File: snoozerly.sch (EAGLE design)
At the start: 49 parts, among them Q1 MOSFET_PCHANNEL, Q2 MOSFET-NCHANNELFDD8780, Q3 MOSFET-NCHANNELBSS123LT1G, Q4 MOSFET-NCHANNELBSS123LT1G, U1 ATMEGA328P, Y1 32KHz, Y2 8MHz

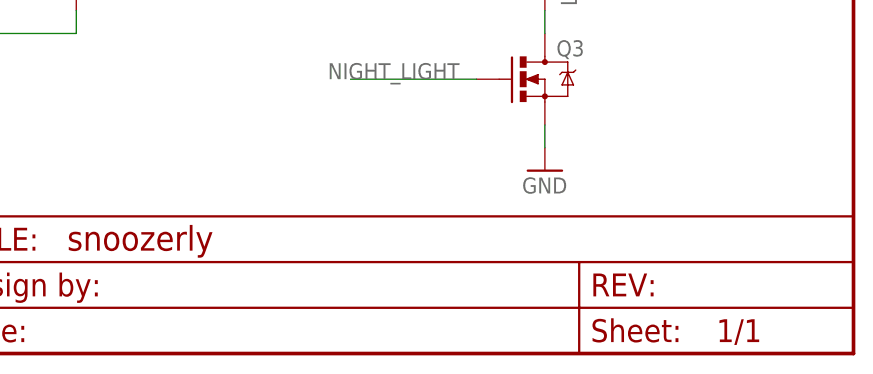
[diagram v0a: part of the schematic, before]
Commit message: renamed board and schematic files
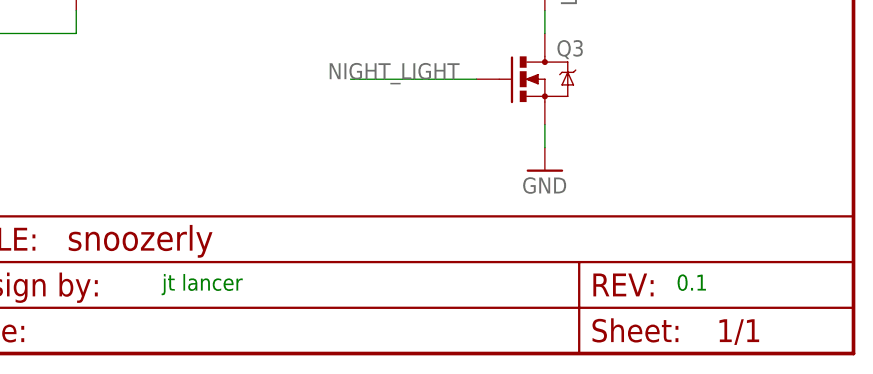
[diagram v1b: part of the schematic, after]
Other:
- note added: "0.1"
- note added: "jt lancer"
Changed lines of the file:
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@@
 <sheet>
 <plain>
+<text x="187.325" y="116.205" size="1.778" layer="91">jt lancer</text>
+<text x="244.475" y="116.205" size="1.778" layer="91">0.1</text>
 </plain>
 <instances>

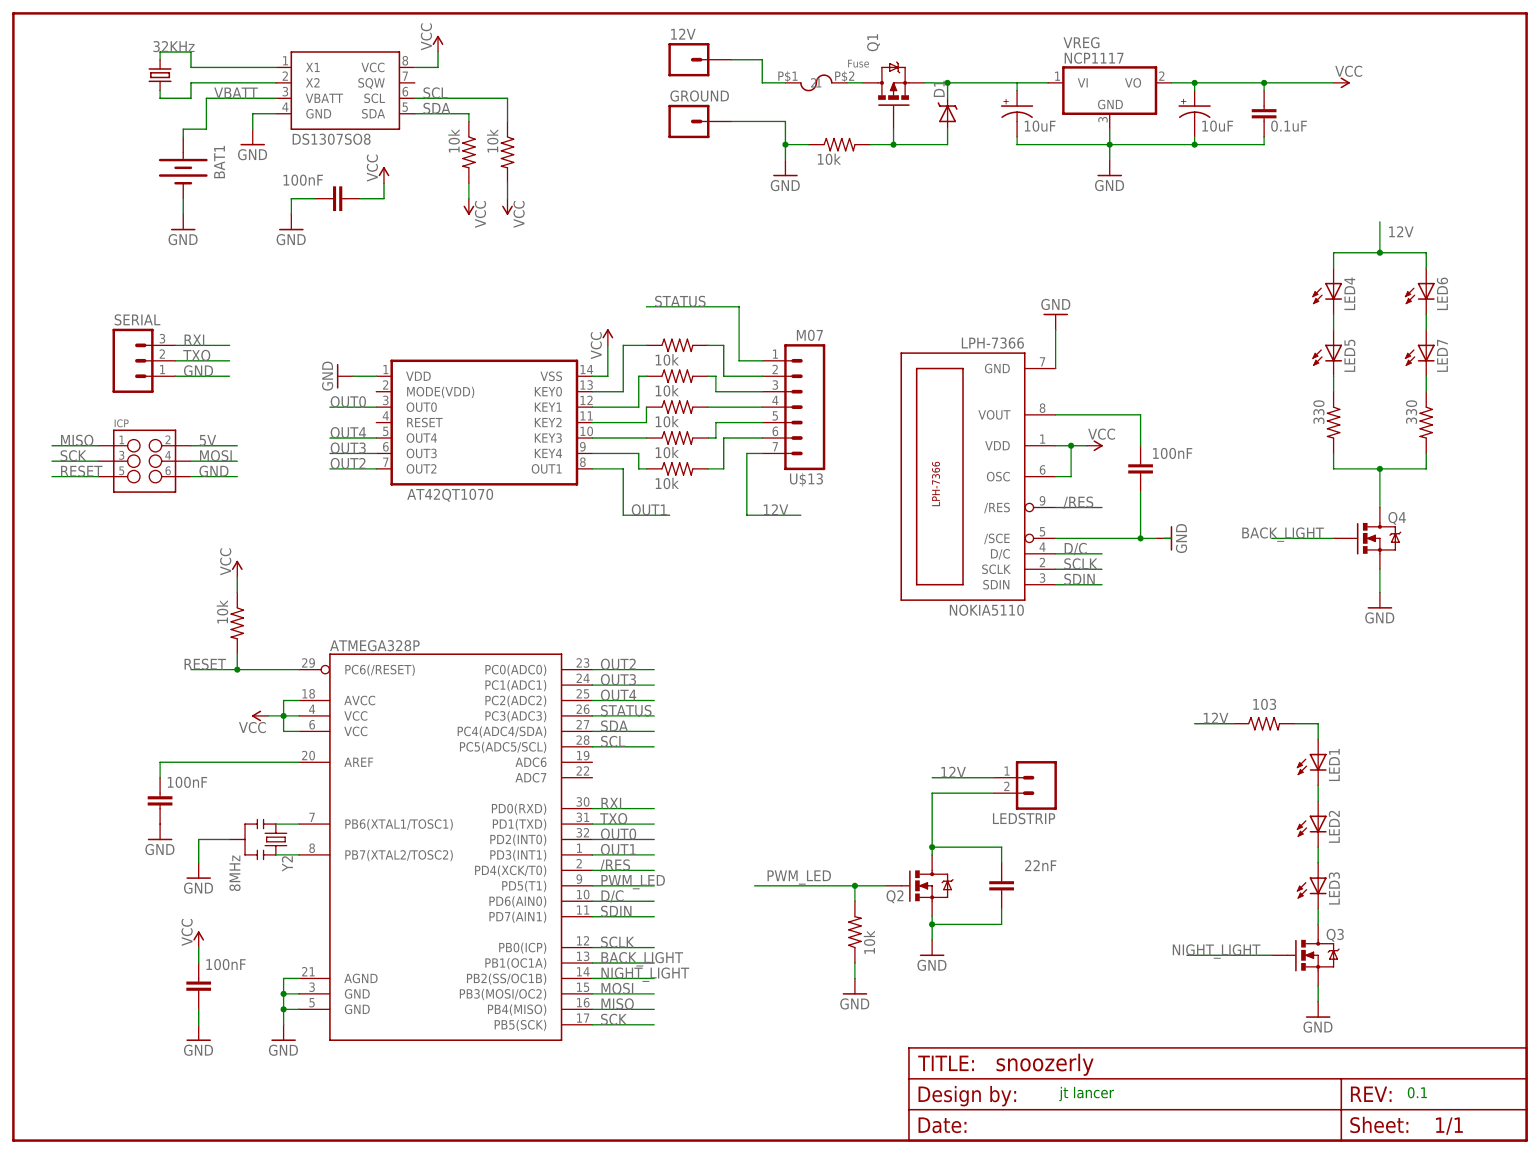
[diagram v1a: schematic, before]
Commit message: added output 0603 pullup resistors to touch sensor.
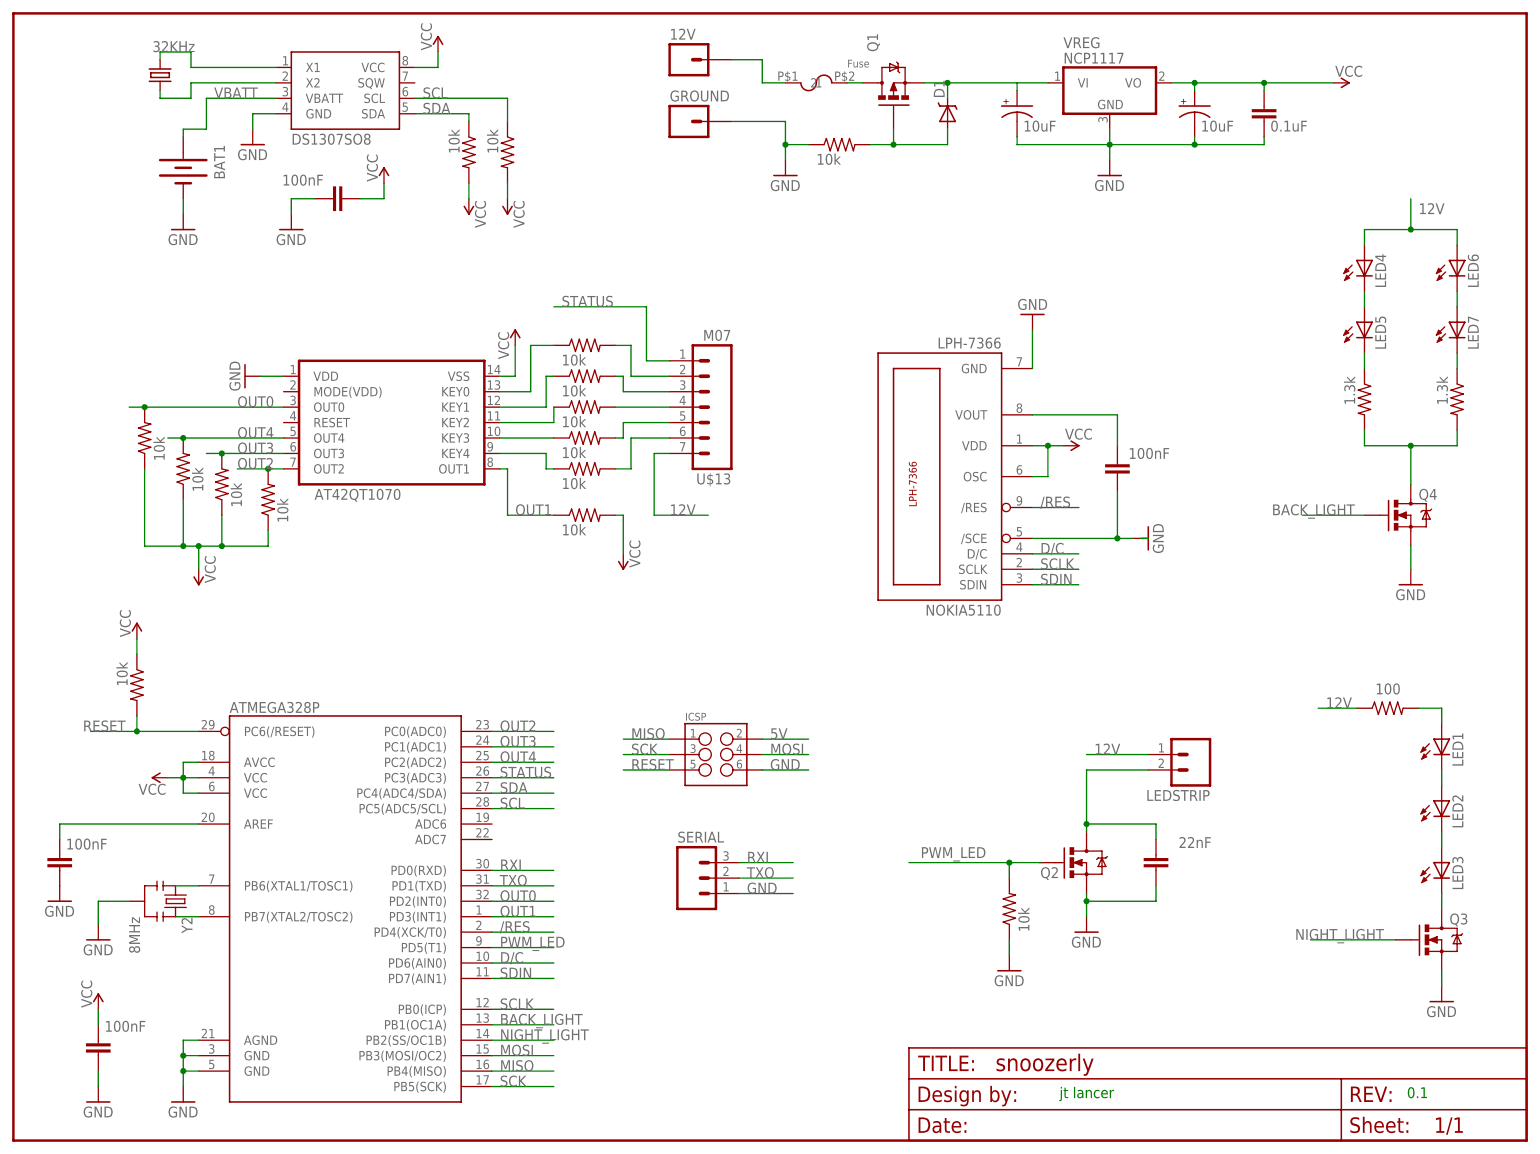
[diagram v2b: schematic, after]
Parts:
- removed ICP: (no value), SparkFun-Connectors:M03X2POGO_PINS
- added ICSP: (no value), SparkFun-Connectors:M03X2POGO_PINS
- added U$21, U$22, U$23, U$24, U$6: 10k, adafruit:R-US_R0603
- U$10, U$11, U$7, U$8, U$9: device jt_parts:RESISTOR -> adafruit:R-US_R0603
- U$16: value 103 -> 100
- U$17, U$18: value 330 -> 1.3k
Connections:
- net 5V: now also ICSP.2, U$21.1, U$22.1, U$23.2, U$24.1, U$6.1; no longer ICP.2
- net GND: now also ICSP.6; no longer ICP.6
- net MISO: now also ICSP.1; no longer ICP.1
- net MOSI: now also ICSP.4; no longer ICP.4
- net OUT0: now also U$6.2
- net OUT1: now also U$23.1
- net OUT2: now also U$22.2
- net OUT3: now also U$21.2
- net OUT4: now also U$24.2
- net RESET: now also ICSP.5; no longer ICP.5
- net SCK: now also ICSP.3; no longer ICP.3
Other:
- moved on the sheet: LED1, LED2, LED3, LED4, LED5, LED6, LED7, LEDSTRIP, NOKIA5110, Q2, Q3, Q4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

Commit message: Added electrolytics and snubber jumper.
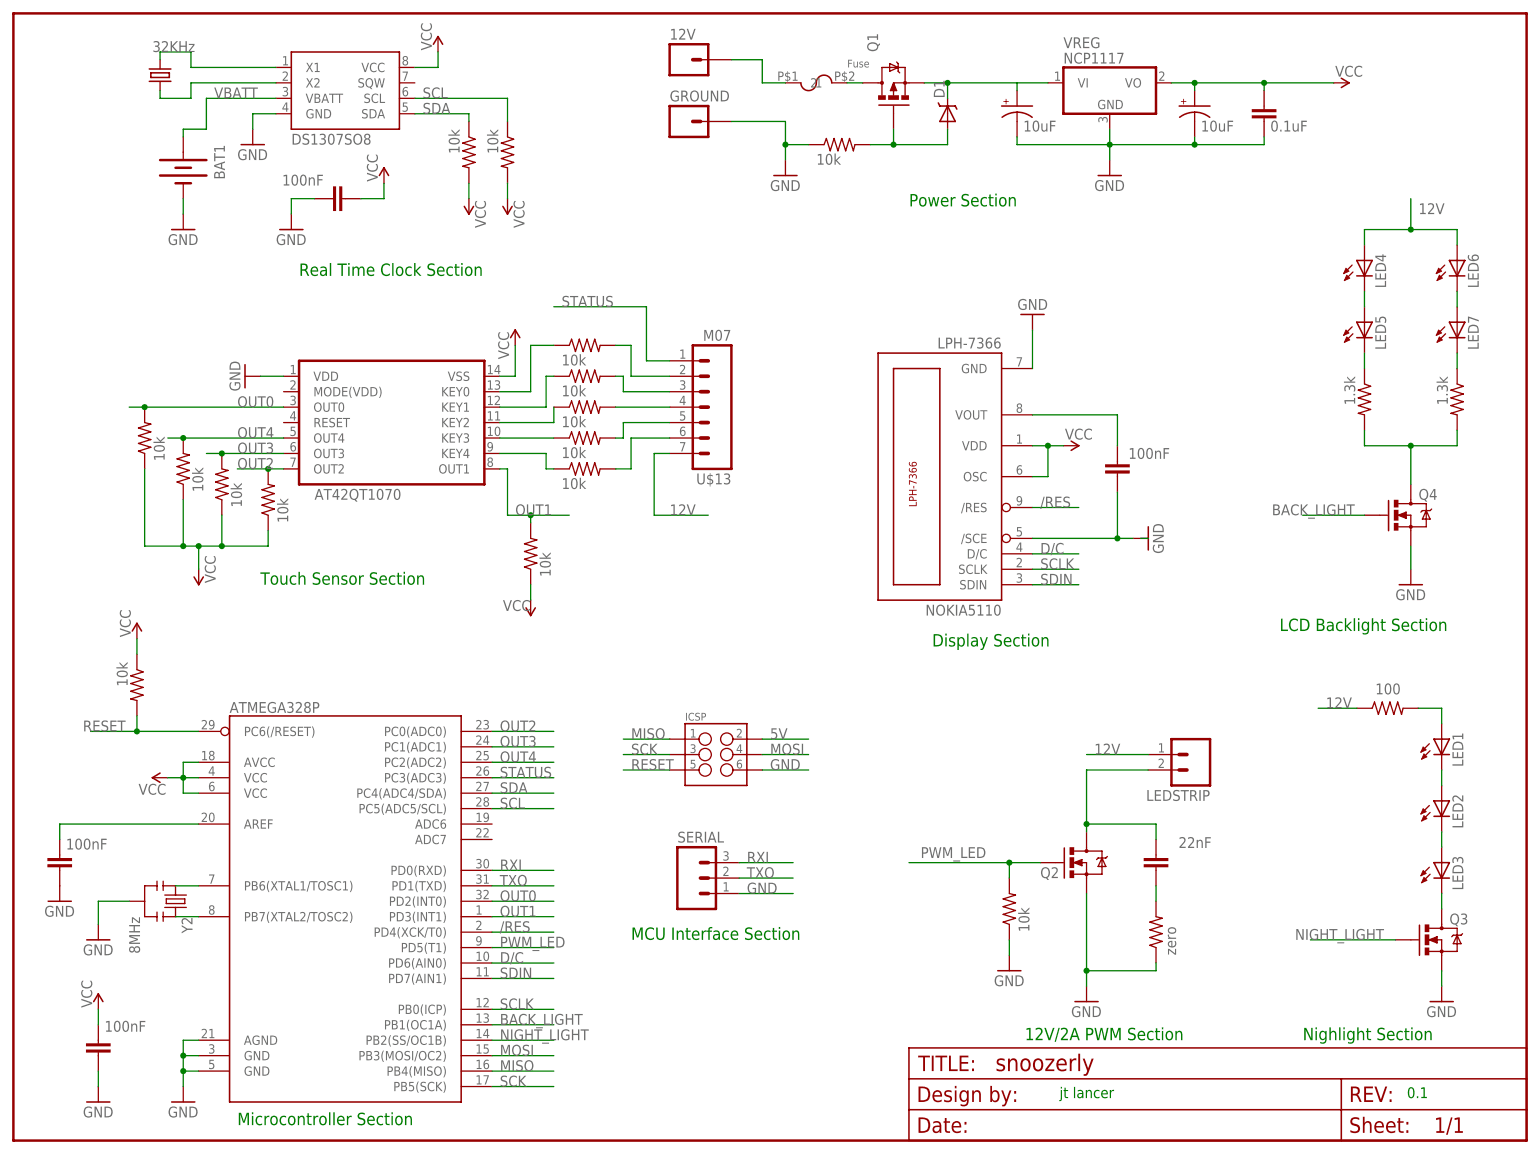
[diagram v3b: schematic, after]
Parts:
- added U$25: zero, adafruit:R-US_R0603
- C5, C7: device SparkFun-Capacitors:CAP_POL1206-KIT -> SparkFun-Capacitors:CAP_POLC
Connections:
- new net N$18: C4.1, U$25.2
- net 5V: now also U$23.1; no longer U$23.2
- net GND: now also U$25.1; no longer C4.1
- net OUT1: now also U$23.2; no longer U$23.1
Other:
- note added: "12V/2A PWM Section"
- note added: "Display Section"
- note added: "LCD Backlight Section"
- note added: "MCU Interface Section"
- note added: "Microcontroller Section"
- note added: "Nighlight Section"
- note added: "Power Section"
- note added: "Real Time Clock Section"
- note added: "Touch Sensor Section"
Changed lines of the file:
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@@
 <part name="LED2" library="jt_parts" deviceset="LED" device="" value=""/>
 <part name="LED3" library="jt_parts" deviceset="LED" device="" value=""/>
-<part name="C5" library="SparkFun-Capacitors" deviceset="CAP_POL" device="1206-KIT" value="10uF"/>
-<part name="C7" library="SparkFun-Capacitors" deviceset="CAP_POL" device="1206-KIT" value="10uF"/>
+<part name="C5" library="SparkFun-Capacitors" deviceset="CAP_POL" device="C" value="10uF"/>
+<part name="C7" library="SparkFun-Capacitors" deviceset="CAP_POL" device="C" value="10uF"/>
 <part name="C2" library="SparkFun-Capacitors" deviceset="CAP" device="0805" value="100nF"/>
 <part name="C1" library="SparkFun-Capacitors" deviceset="CAP" device="0805" value="100nF"/>
@@
 <part name="U$13" library="jt_parts" deviceset="M07" device=""/>
 <part name="U$23" library="adafruit" deviceset="R-US_" device="R0603" value="10k"/>
-<part name="SUPPLY6" library="SparkFun-Aesthetics" deviceset="VCC" device=""/>
+<part name="SUPPLY6" library="SparkFun-Aesthetics" deviceset="VCC" device="">
+<attribute name="VCC" value="VCC"/>
+</part>
 <part name="U$6" library="adafruit" deviceset="R-US_" device="R0603" value="10k"/>
 <part name="U$21" library="adafruit" deviceset="R-US_" device="R0603" value="10k"/>
@@
 <part name="U$24" library="adafruit" deviceset="R-US_" device="R0603" value="10k"/>
 <part name="SUPPLY11" library="SparkFun-Aesthetics" deviceset="VCC" device=""/>
+<part name="U$25" library="adafruit" deviceset="R-US_" device="R0603" value="zero"/>
 </parts>
 <sheets>
@@
 <text x="187.325" y="116.205" size="1.778" layer="91">jt lancer</text>
 <text x="244.475" y="116.205" size="1.778" layer="91">0.1</text>
+<text x="62.23" y="251.46" size="2.032" layer="91">Real Time Clock Section</text>
+<text x="55.88" y="200.66" size="2.032" layer="91">Touch Sensor Section</text>
+<text x="52.07" y="111.76" size="2.032" layer="91">Microcontroller Section</text>
+<text x="116.84" y="142.24" size="2.032" layer="91">MCU Interface Section</text>
+<text x="181.61" y="125.73" size="2.032" layer="91">12V/2A PWM Section</text>
+<text x="227.33" y="125.73" size="2.032" layer="91">Nighlight Section</text>
+<text x="223.52" y="193.04" size="2.032" layer="91" ratio="10">LCD Backlight Section</text>
+<text x="166.37" y="190.5" size="2.032" layer="91">Display Section</text>
+<text x="162.56" y="262.89" size="2.032" layer="91">Power Section</text>
 </plain>
 <instances>
@@
 <instance part="GND2" gate="1" x="142.24" y="267.97"/>
 <instance part="GND4" gate="1" x="195.58" y="267.97"/>
-<instance part="GND6" gate="1" x="191.77" y="143.51"/>
+<instance part="GND6" gate="1" x="191.77" y="132.08"/>
 <instance part="LEDSTRIP" gate="G$1" x="209.55" y="172.72" smashed="yes" rot="R180">
 <attribute name="NAME" x="212.09" y="166.878" size="1.778" layer="95" rot="R180"/>
@@
 </instance>
 <instance part="U$13" gate="G$1" x="128.27" y="229.87" rot="R180"/>
-<instance part="U$23" gate="G$1" x="109.22" y="212.09" smashed="yes">
-<attribute name="VALUE" x="105.41" y="208.788" size="1.778" layer="96"/>
-</instance>
-<instance part="SUPPLY6" gate="1" x="115.57" y="205.74" smashed="yes" rot="R180">
-<attribute name="VALUE" x="116.586" y="208.026" size="1.778" layer="96" rot="R270"/>
+<instance part="U$23" gate="G$1" x="100.33" y="205.74" smashed="yes" rot="R90">
+<attribute name="VALUE" x="103.632" y="201.93" size="1.778" layer="96" rot="R90"/>
+</instance>
+<instance part="SUPPLY6" gate="1" x="100.33" y="198.12" smashed="yes" rot="R180">
+<attribute name="VCC" x="100.33" y="198.12" size="1.778" layer="96" rot="R180"/>
 </instance>
 <instance part="U$6" gate="G$1" x="36.83" y="224.79" smashed="yes" rot="R90">
@@
 <instance part="SUPPLY11" gate="1" x="45.72" y="203.2" smashed="yes" rot="R180">
 <attribute name="VALUE" x="46.736" y="205.486" size="1.778" layer="96" rot="R270"/>
+</instance>
+<instance part="U$25" gate="G$1" x="203.2" y="143.51" smashed="yes" rot="R90">
+<attribute name="VALUE" x="206.502" y="139.7" size="1.778" layer="96" rot="R90"/>
 </instance>
 </instances>
@@
 <segment>
 <pinref part="Q2" gate="G$1" pin="S"/>
-<wire x1="191.77" y1="149.86" x2="191.77" y2="148.59" width="0.1524" layer="91"/>
-<wire x1="191.77" y1="148.59" x2="203.2" y2="148.59" width="0.1524" layer="91"/>
-<pinref part="C4" gate="G$1" pin="1"/>
-<wire x1="203.2" y1="148.59" x2="203.2" y2="151.13" width="0.1524" layer="91"/>
+<wire x1="191.77" y1="149.86" x2="191.77" y2="137.16" width="0.1524" layer="91"/>
 <pinref part="GND6" gate="1" pin="GND"/>
-<wire x1="191.77" y1="148.59" x2="191.77" y2="146.05" width="0.1524" layer="91"/>
-<junction x="191.77" y="148.59"/>
+<pinref part="U$25" gate="G$1" pin="1"/>
+<wire x1="191.77" y1="137.16" x2="191.77" y2="134.62" width="0.1524" layer="91"/>
+<wire x1="203.2" y1="138.43" x2="203.2" y2="137.16" width="0.1524" layer="91"/>
+<wire x1="203.2" y1="137.16" x2="191.77" y2="137.16" width="0.1524" layer="91"/>
+<junction x="191.77" y="137.16"/>
 </segment>
 <segment>
@@
 </segment>
 <segment>
-<pinref part="U$23" gate="G$1" pin="2"/>
-<wire x1="114.3" y1="212.09" x2="115.57" y2="212.09" width="0.1524" layer="91"/>
-<wire x1="115.57" y1="212.09" x2="115.57" y2="205.74" width="0.1524" layer="91"/>
+<pinref part="U$23" gate="G$1" pin="1"/>
 <pinref part="SUPPLY6" gate="1" pin="VCC"/>
+<wire x1="100.33" y1="200.66" x2="100.33" y2="198.12" width="0.1524" layer="91"/>
 </segment>
 </net>
@@
 <wire x1="95.25" y1="219.71" x2="96.52" y2="219.71" width="0.1524" layer="91"/>
 <wire x1="96.52" y1="219.71" x2="96.52" y2="212.09" width="0.1524" layer="91"/>
-<wire x1="96.52" y1="212.09" x2="104.14" y2="212.09" width="0.1524" layer="91"/>
 <label x="97.79" y="212.09" size="1.778" layer="95"/>
-<pinref part="U$23" gate="G$1" pin="1"/>
+<wire x1="96.52" y1="212.09" x2="100.33" y2="212.09" width="0.1524" layer="91"/>
+<pinref part="U$23" gate="G$1" pin="2"/>
+<wire x1="100.33" y1="212.09" x2="106.68" y2="212.09" width="0.1524" layer="91"/>
+<wire x1="100.33" y1="212.09" x2="100.33" y2="210.82" width="0.1524" layer="91"/>
+<junction x="100.33" y="212.09"/>
 </segment>
 <segment>
@@
 </segment>
 </net>
+<net name="N$18" class="0">
+<segment>
+<pinref part="C4" gate="G$1" pin="1"/>
+<pinref part="U$25" gate="G$1" pin="2"/>
+<wire x1="203.2" y1="151.13" x2="203.2" y2="148.59" width="0.1524" layer="91"/>
+</segment>
+</net>
